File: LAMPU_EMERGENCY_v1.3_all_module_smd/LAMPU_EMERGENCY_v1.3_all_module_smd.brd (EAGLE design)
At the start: 134.3 x 67.3 mm, 62 parts, among them Q1 IRF540D2PACK, T1 SS8050, T4 SS8050, T5 SS8050, T6 SS8050, T8 SS8050, X1 BATTERY_1, X2 AC_PIN, X3 MOSOUT, X4 BATTERY2, X6 MOSOUT, X7 AC_PIN

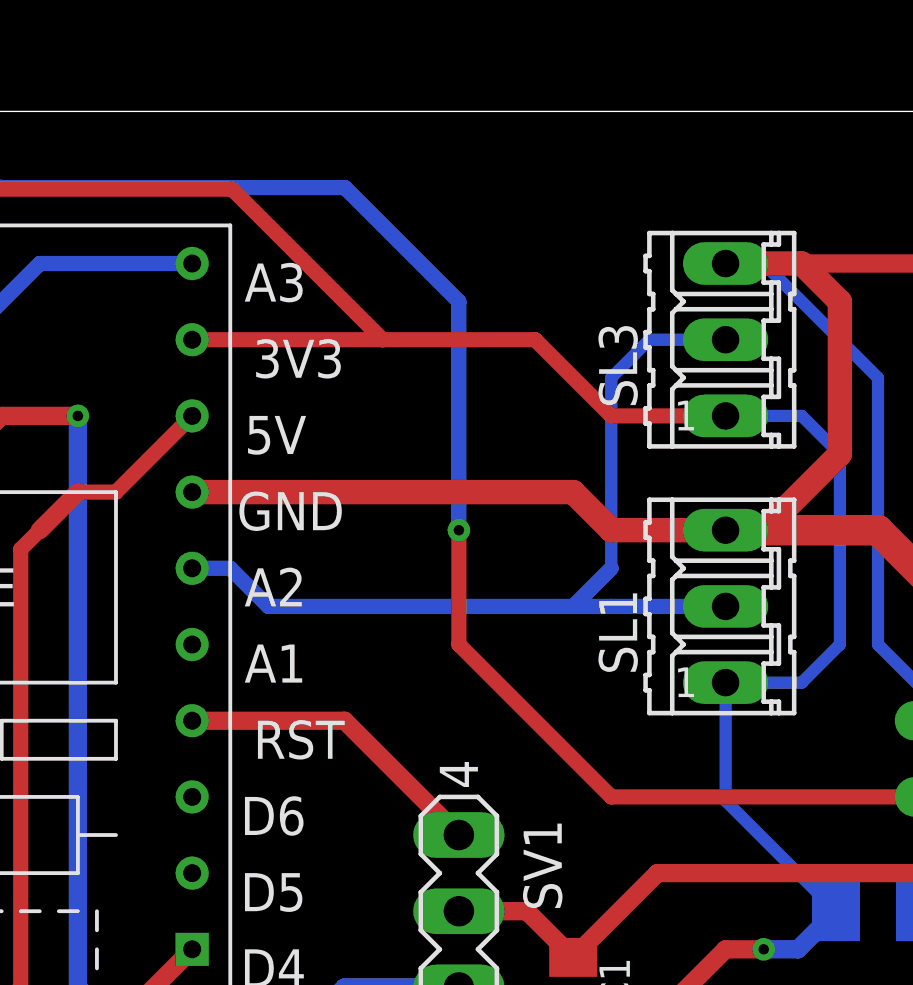
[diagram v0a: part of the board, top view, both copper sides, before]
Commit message: Split X and Y vibration sensors
separate it, maybe someone use sensors have different type
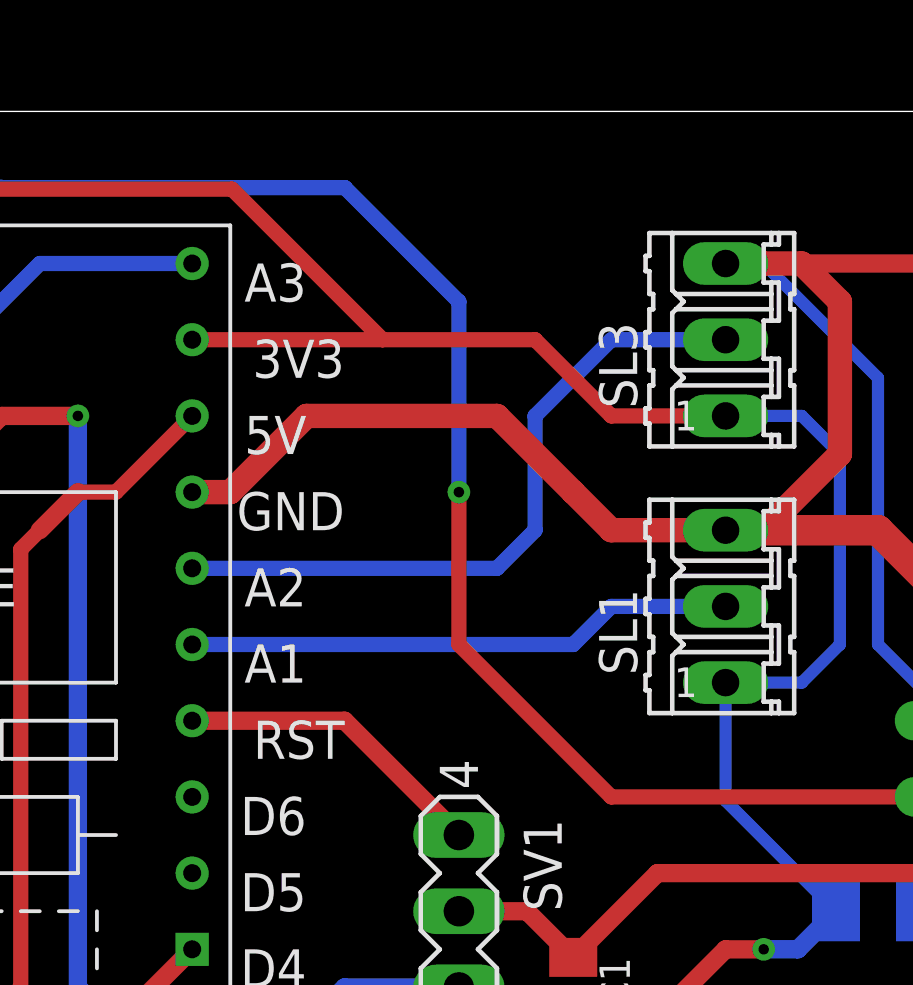
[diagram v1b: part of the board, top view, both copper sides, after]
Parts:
- SL1: value VIBRATION_X -> VIBRATION_Y
- SL3: value VIBRATION_Y -> VIBRATION_X
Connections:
- removed net VIB_SEN: SL1.2, SL3.2, U$2.A2
- new net VIB_SEN_X: SL3.2, U$2.A2
- new net VIB_SEN_Y: SL1.2, U$2.A1
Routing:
- net VIB_SEN: track 32.1 -> 0.00 mm
- net VIB_SEN_X: track 0.00 -> 23.2 mm
- net VIB_SEN_Y: track 0.00 -> 19.6 mm
- net GND: track 616.3 -> 618.4 mm
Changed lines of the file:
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@@
 <grid distance="50" unitdist="mil" unit="mil" style="lines" multiple="1" display="no" altdistance="5" altunitdist="mil" altunit="mil"/>
 <layers>
-<layer number="1" name="Top" color="4" fill="1" visible="no" active="yes"/>
+<layer number="1" name="Top" color="4" fill="1" visible="yes" active="yes"/>
 <layer number="2" name="Route2" color="16" fill="1" visible="no" active="no"/>
 <layer number="3" name="Route3" color="17" fill="1" visible="no" active="no"/>
@@
 <layer number="14" name="Route14" color="22" fill="1" visible="no" active="no"/>
 <layer number="15" name="Route15" color="23" fill="1" visible="no" active="no"/>
-<layer number="16" name="Bottom" color="1" fill="1" visible="no" active="yes"/>
+<layer number="16" name="Bottom" color="1" fill="1" visible="yes" active="yes"/>
 <layer number="17" name="Pads" color="2" fill="1" visible="yes" active="yes"/>
 <layer number="18" name="Vias" color="2" fill="1" visible="yes" active="yes"/>
@@
 <wire x1="-34.29" y1="73.65" x2="-34.29" y2="6.35" width="0" layer="20"/>
 <polygon width="0.1524" layer="41">
-<vertex x="100.33" y="64.77"/>
+<vertex x="99.06" y="64.77"/>
 <vertex x="67.31" y="64.77"/>
-<vertex x="62.23" y="59.69"/>
-<vertex x="62.23" y="26.67"/>
+<vertex x="60.96" y="58.42"/>
+<vertex x="60.96" y="27.94"/>
 <vertex x="68.58" y="20.32"/>
-<vertex x="100.33" y="20.32"/>
-<vertex x="100.33" y="21.59"/>
+<vertex x="99.06" y="20.32"/>
+<vertex x="99.06" y="21.59"/>
 <vertex x="68.58" y="21.59"/>
-<vertex x="63.5" y="26.67"/>
-<vertex x="63.5" y="58.42"/>
+<vertex x="62.23" y="27.94"/>
+<vertex x="62.23" y="57.15"/>
 <vertex x="68.58" y="63.5"/>
-<vertex x="100.33" y="63.5"/>
+<vertex x="99.06" y="63.5"/>
 </polygon>
 <polygon width="0.1524" layer="42">
-<vertex x="100.33" y="21.59"/>
-<vertex x="100.33" y="20.32"/>
+<vertex x="99.06" y="21.59"/>
+<vertex x="99.06" y="20.32"/>
 <vertex x="68.58" y="20.32"/>
-<vertex x="62.23" y="26.67"/>
-<vertex x="62.23" y="59.69"/>
+<vertex x="60.96" y="27.94"/>
+<vertex x="60.96" y="58.42"/>
 <vertex x="67.31" y="64.77"/>
-<vertex x="100.33" y="64.77"/>
-<vertex x="100.33" y="63.5"/>
+<vertex x="99.06" y="64.77"/>
+<vertex x="99.06" y="63.5"/>
 <vertex x="68.58" y="63.5"/>
-<vertex x="63.5" y="58.42"/>
-<vertex x="63.5" y="26.67"/>
+<vertex x="62.23" y="57.15"/>
+<vertex x="62.23" y="27.94"/>
 <vertex x="68.58" y="21.59"/>
 </polygon>
@@
 <attribute name="VALUE" x="90.17" y="43.688" size="1.27" layer="27" ratio="10"/>
 </element>
-<element name="SL1" library="con-amp-quick" library_urn="urn:adsk.eagle:library:125" package="03P" package3d_urn="urn:adsk.eagle:package:5957/1" value="VIBRATION_X" x="49.53" y="57.15" smashed="yes" rot="R90">
+<element name="SL1" library="con-amp-quick" library_urn="urn:adsk.eagle:library:125" package="03P" package3d_urn="urn:adsk.eagle:package:5957/1" value="VIBRATION_Y" x="49.53" y="57.15" smashed="yes" rot="R90">
 <attribute name="MF" value="" x="129.54" y="125.73" size="1.778" layer="27" rot="R90" display="off"/>
 <attribute name="MPN" value="" x="129.54" y="125.73" size="1.778" layer="27" rot="R90" display="off"/>
@@
 <attribute name="VALUE" x="7.874" y="64.7446" size="1.27" layer="27" ratio="10"/>
 </element>
-<element name="SL3" library="con-amp-quick" library_urn="urn:adsk.eagle:library:125" package="03P" package3d_urn="urn:adsk.eagle:package:5957/1" value="VIBRATION_Y" x="49.53" y="66.04" smashed="yes" rot="R90">
+<element name="SL3" library="con-amp-quick" library_urn="urn:adsk.eagle:library:125" package="03P" package3d_urn="urn:adsk.eagle:package:5957/1" value="VIBRATION_X" x="49.53" y="66.04" smashed="yes" rot="R90">
 <attribute name="MF" value="" x="129.54" y="148.59" size="1.778" layer="27" rot="R90" display="off"/>
 <attribute name="MPN" value="" x="129.54" y="148.59" size="1.778" layer="27" rot="R90" display="off"/>
@@
 <wire x1="40.64" y1="24.13" x2="36.7" y2="28.07" width="1.016" layer="16"/>
 <wire x1="35.56" y1="28.07" x2="36.7" y2="28.07" width="1.016" layer="16"/>
-<wire x1="31.75" y1="60.96" x2="44.45" y2="60.96" width="0.8128" layer="1"/>
+<wire x1="31.75" y1="60.96" x2="33.02" y2="60.96" width="0.8128" layer="1"/>
 <wire x1="44.45" y1="60.96" x2="45.72" y2="59.69" width="0.8128" layer="1"/>
 <wire x1="45.72" y1="59.69" x2="49.53" y2="59.69" width="0.8128" layer="1"/>
@@
 <wire x1="44.45" y1="45.45" x2="47.26" y2="48.26" width="0.6096" layer="1"/>
 <wire x1="47.26" y1="48.26" x2="59.69" y2="48.26" width="0.6096" layer="1"/>
+<wire x1="33.02" y1="60.96" x2="35.56" y2="63.5" width="0.8128" layer="1"/>
+<wire x1="35.56" y1="63.5" x2="41.91" y2="63.5" width="0.8128" layer="1"/>
+<wire x1="41.91" y1="63.5" x2="44.45" y2="60.96" width="0.8128" layer="1"/>
 </signal>
 <signal name="+3V3">
@@
 <wire x1="33.0808" y1="71.0592" x2="38.1" y2="66.04" width="0.508" layer="1"/>
 <wire x1="10.16" y1="71.0592" x2="33.0808" y2="71.0592" width="0.508" layer="1"/>
-</signal>
-<signal name="VIB_SEN">
-<contactref element="U$2" pad="A2"/>
-<contactref element="SL1" pad="2"/>
-<contactref element="SL3" pad="2"/>
-<wire x1="49.53" y1="66.04" x2="46.99" y2="66.04" width="0.4064" layer="16"/>
-<wire x1="46.99" y1="66.04" x2="45.72" y2="64.77" width="0.4064" layer="16"/>
-<wire x1="46.99" y1="57.15" x2="48.26" y2="57.15" width="0.4064" layer="16"/>
-<wire x1="48.26" y1="57.15" x2="49.53" y2="57.15" width="0.4064" layer="16"/>
-<wire x1="45.72" y1="64.77" x2="45.72" y2="58.42" width="0.4064" layer="16"/>
-<wire x1="31.75" y1="58.42" x2="33.02" y2="58.42" width="0.508" layer="16"/>
-<wire x1="33.02" y1="58.42" x2="34.29" y2="57.15" width="0.508" layer="16"/>
-<wire x1="34.29" y1="57.15" x2="44.45" y2="57.15" width="0.508" layer="16"/>
-<wire x1="44.45" y1="57.15" x2="45.72" y2="57.15" width="0.508" layer="16"/>
-<wire x1="45.72" y1="57.15" x2="48.26" y2="57.15" width="0.508" layer="16"/>
-<wire x1="45.72" y1="58.42" x2="44.45" y2="57.15" width="0.508" layer="16"/>
 </signal>
 <signal name="BAT1">
@@
 <wire x1="19.05" y1="55.88" x2="20.955" y2="57.785" width="0.508" layer="16"/>
 <wire x1="25.4" y1="71.11" x2="36.84" y2="71.11" width="0.508" layer="16"/>
-<wire x1="36.84" y1="71.11" x2="40.64" y2="67.31" width="0.508" layer="16"/>
-<wire x1="40.64" y1="67.31" x2="40.64" y2="59.69" width="0.508" layer="16"/>
-<via x="40.64" y="59.69" extent="1-16" drill="0.35"/>
-<wire x1="40.64" y1="59.69" x2="40.64" y2="55.88" width="0.508" layer="1"/>
-<wire x1="40.64" y1="55.88" x2="45.72" y2="50.8" width="0.508" layer="1"/>
+<wire x1="40.64" y1="67.31" x2="36.84" y2="71.11" width="0.508" layer="16"/>
+<wire x1="45.72" y1="50.8" x2="40.64" y2="55.88" width="0.508" layer="1"/>
 <wire x1="45.72" y1="50.8" x2="57.15" y2="50.8" width="0.508" layer="1"/>
 <wire x1="20.955" y1="57.785" x2="20.955" y2="67.945" width="0.508" layer="16"/>
@@
 <wire x1="24.13" y1="71.12" x2="25.39" y2="71.12" width="0.508" layer="16"/>
 <wire x1="25.39" y1="71.12" x2="25.4" y2="71.11" width="0.508" layer="16"/>
+<wire x1="40.64" y1="55.88" x2="40.64" y2="60.96" width="0.508" layer="1"/>
+<via x="40.64" y="60.96" extent="1-16" drill="0.35"/>
+<wire x1="40.64" y1="60.96" x2="40.64" y2="67.31" width="0.508" layer="16"/>
 </signal>
 <signal name="N$3">
@@
 <wire x1="36.83" y1="53.34" x2="31.75" y2="53.34" width="0.6096" layer="1"/>
 </signal>
+<signal name="VIB_SEN_X">
+<contactref element="U$2" pad="A2"/>
+<contactref element="SL3" pad="2"/>
+<wire x1="41.91" y1="58.42" x2="31.75" y2="58.42" width="0.508" layer="16"/>
+<wire x1="43.18" y1="59.69" x2="41.91" y2="58.42" width="0.508" layer="16"/>
+<wire x1="49.53" y1="66.04" x2="45.72" y2="66.04" width="0.508" layer="16"/>
+<wire x1="45.72" y1="66.04" x2="43.18" y2="63.5" width="0.508" layer="16"/>
+<wire x1="43.18" y1="63.5" x2="43.18" y2="59.69" width="0.508" layer="16"/>
+</signal>
+<signal name="VIB_SEN_Y">
+<contactref element="U$2" pad="A1"/>
+<contactref element="SL1" pad="2"/>
+<wire x1="48.26" y1="57.15" x2="49.53" y2="57.15" width="0.4064" layer="16"/>
+<wire x1="44.45" y1="55.88" x2="45.72" y2="57.15" width="0.508" layer="16"/>
+<wire x1="45.72" y1="57.15" x2="49.53" y2="57.15" width="0.508" layer="16"/>
+<wire x1="31.75" y1="55.88" x2="44.45" y2="55.88" width="0.508" layer="16"/>
+</signal>
 </signals>
